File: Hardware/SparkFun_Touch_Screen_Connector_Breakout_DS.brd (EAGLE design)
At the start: 12.7 x 12.7 mm, 3 parts

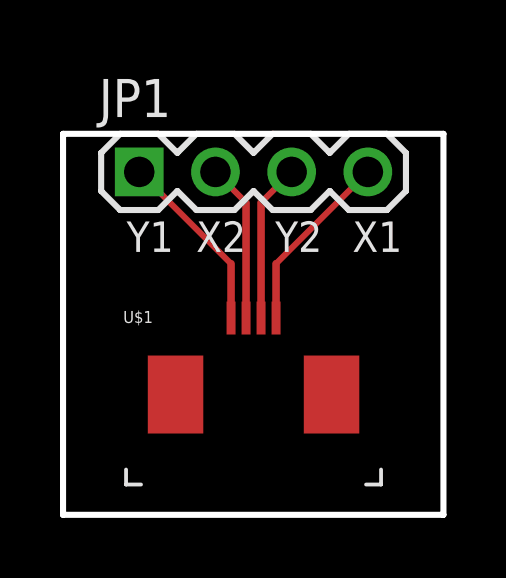
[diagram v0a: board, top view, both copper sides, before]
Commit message: added board fiducials
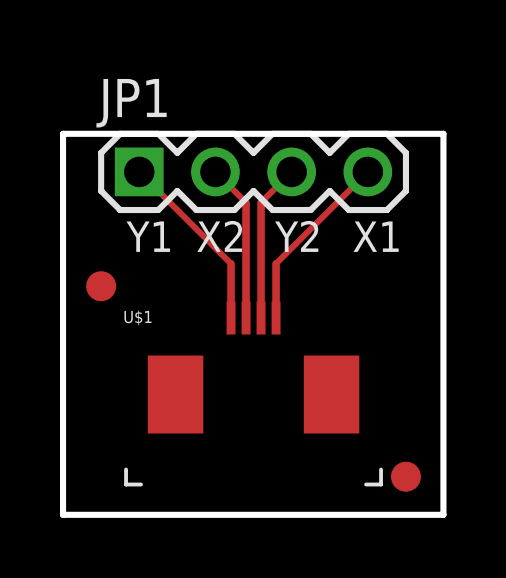
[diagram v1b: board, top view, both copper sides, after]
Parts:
- added FID1, FID2: FIDUCIAL1X2, SparkFun-Aesthetics:FIDUCIAL-1X2
